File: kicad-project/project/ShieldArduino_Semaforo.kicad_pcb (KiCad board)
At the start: 4 copper layers, 68.6 x 53.3 mm, 108 parts, among them IC1 TLIN1039DDFRQ1, IC2 TPS563200DDCR, IC3 MCP4901T-E_MS, J2 Conn_01x18, K1 RELAY, P1 Power, P2 Analog, P3 Digital, P4 Digital, P5 CONN_01X01, P6 CONN_01X01, P7 CONN_01X01, P8 CONN_01X01, Q1 PMOS, Q2 NMOS, Q3 NMOS, Q4 NMOS, Q5 NMOS, U1 MCP2542FD-E/MF, U3 LM4040DBZ-2.0

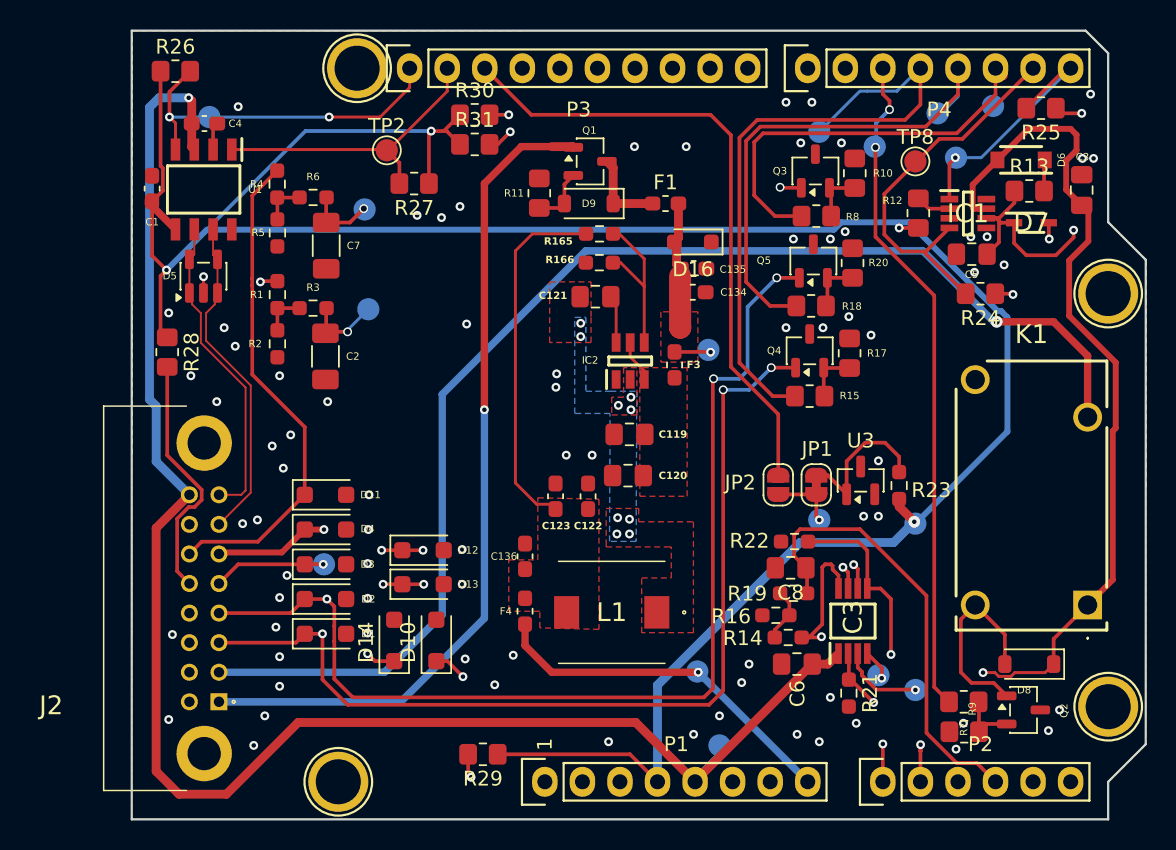
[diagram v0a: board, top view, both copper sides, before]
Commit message: kicad-pcb-silk_layer_cleanup
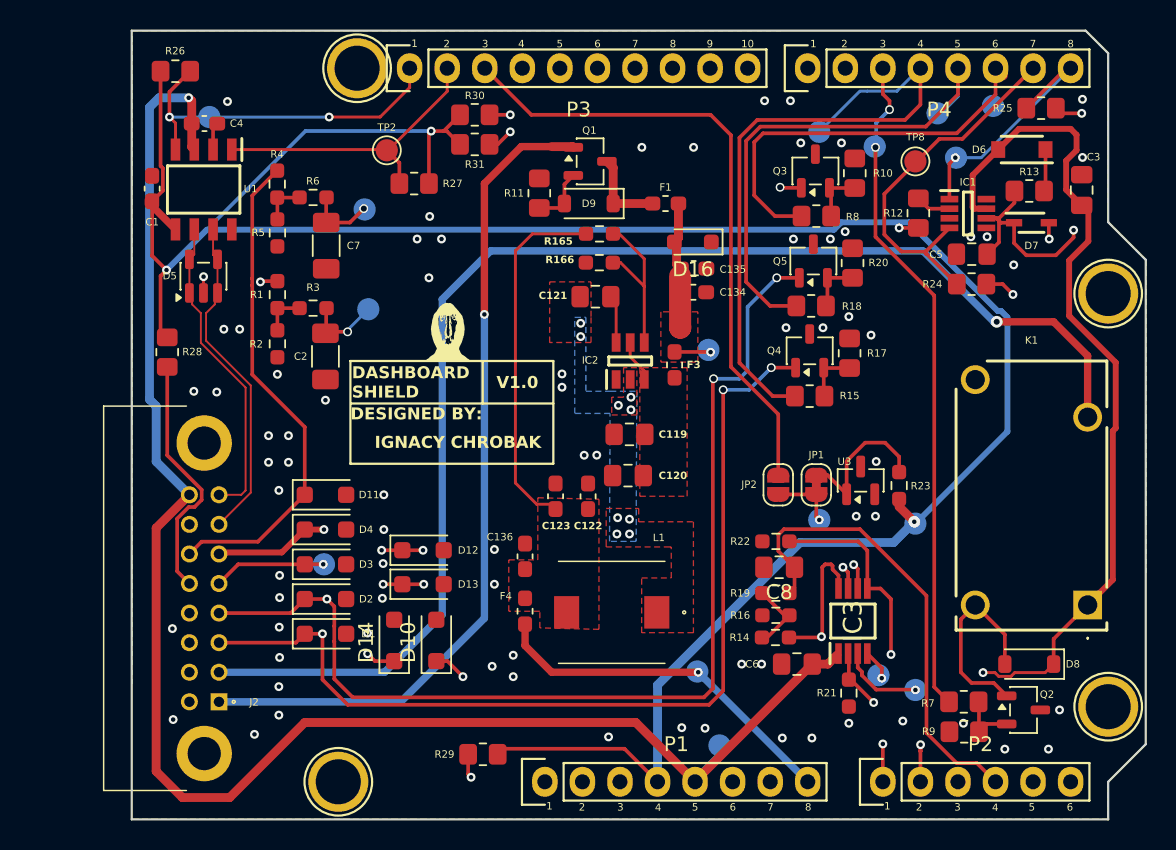
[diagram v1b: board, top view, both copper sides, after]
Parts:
- added G***: LOGO, Graphics:mandela, F.Cu at (132.4, 92.8)
- moved R22 1.26 mm to (154.6, 107.6)
- moved R19 1.20 mm to (154.6, 111.1)
- moved R24 0.88 mm to (167.8, 90.2)
- moved R14 0.86 mm to (154.5, 114.1)
- moved C8 0.78 mm to (154.8, 109.3)
- moved D6 0.70 mm to (171.2, 81.1)
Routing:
- net /relay_out: track 86.4 -> 90.1 mm
- net /STM_LDAC: track 70.8 -> 72.0 mm
- net /A3: track 30.6 -> 31.9 mm
- net Net-(R14-Pad2): track 3.68 -> 4.92 mm
- net +3.3V: track 249.6 -> 250.8 mm
- net /UART_RX: track 25.8 -> 25.0 mm
- net Net-(D6-K): track 2.12 -> 2.84 mm
- net GND: vias 79 -> 76
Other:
- board text added: "10"
- board text added: "2"
- board text added: "3"
- board text added: "4"
- board text added: "5"
- board text added: "6"
- board text added: "7"
- board text added: "8"
- board text added: "9"
- board text added: "DASHBOARD SHIELD"
- board text added: "DESIGNED BY:"
- board text added: "IGNACY CHROBAK"
- board text added: "V1.0"

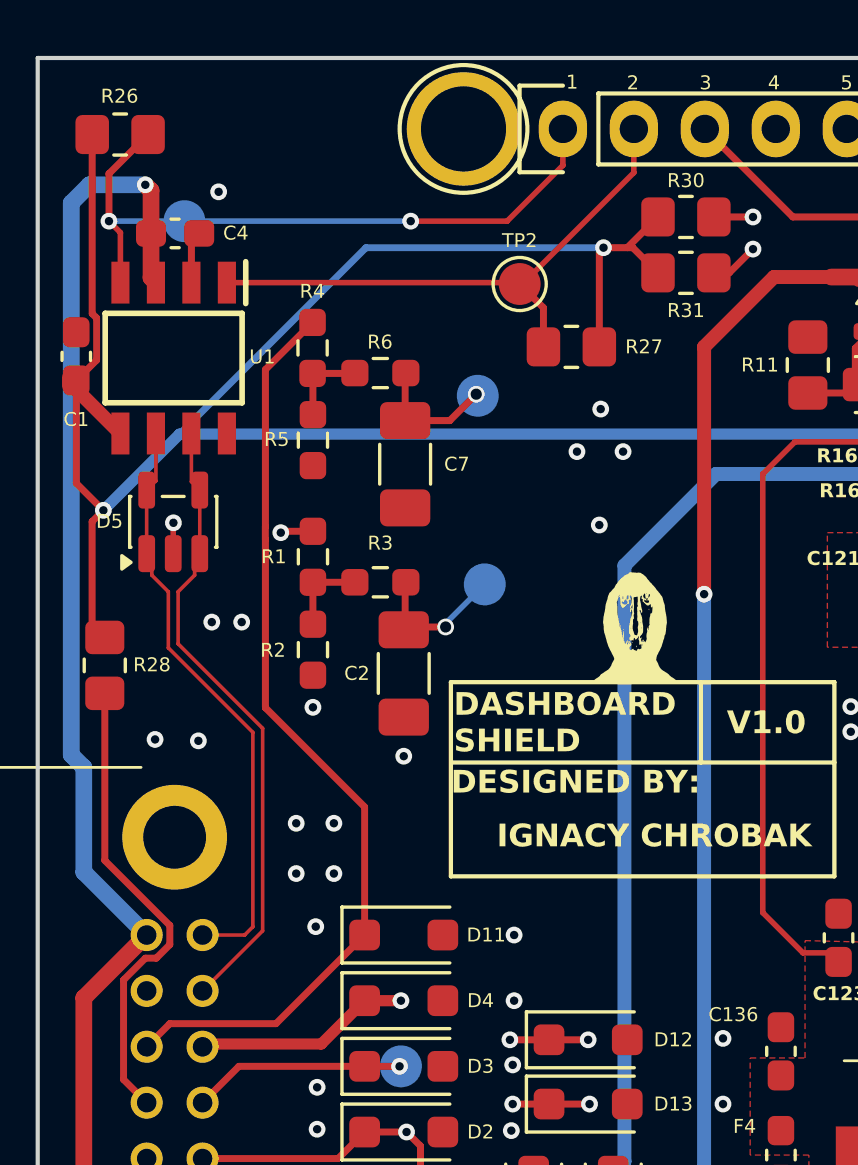
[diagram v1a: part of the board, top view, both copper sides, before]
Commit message: kicad-pcb-images
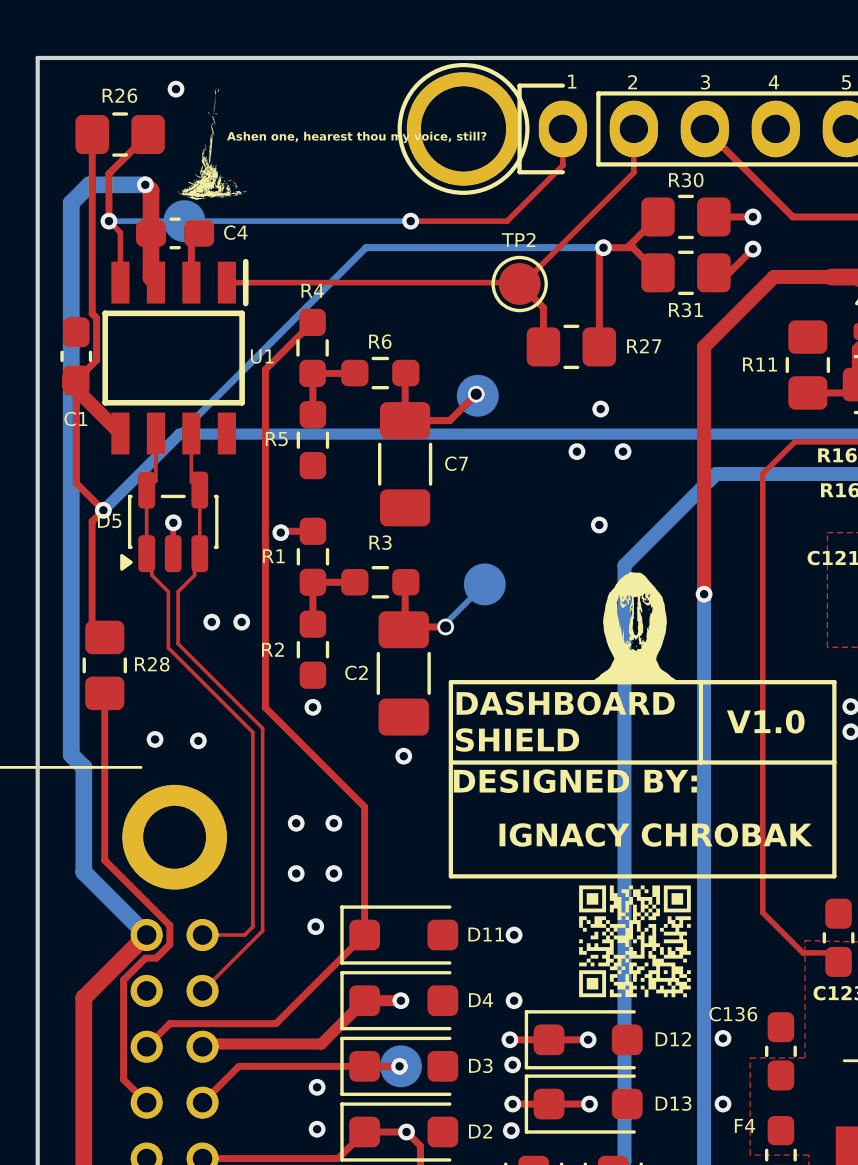
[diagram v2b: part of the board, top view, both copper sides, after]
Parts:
- added G***: LOGO, Graphics:bonfire, F.Cu at (117.2, 76.2)
- added G***: LOGO, Graphics:qr, F.Cu at (132.4, 104.6)
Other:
- board text added: "Ashen one, hearest thou my voice, still?"

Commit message: kicad-images
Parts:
- added G***: LOGO, Graphics:robot, F.Cu at (136.2, 104.4)
- moved G*** 4.90 mm to (137.3, 92.8)
- moved R6 0.24 mm to (123.0, 84.4)

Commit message: .
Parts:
- moved G*** 13.1 mm to (131.1, 116.5)

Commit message: kicad-pcb-relay_change
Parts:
- K1: footprint footprint:PR412V4501A -> footprint:RE034012
- moved K1 17.2 mm to (174.5, 94.7)
- moved R6 0.26 mm to (123.3, 84.4)
- moved C7 0.14 mm to (124.1, 87.7)
- moved R5 0.13 mm to (120.8, 86.8)
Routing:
- net /12V_in_protected: track 104.5 -> 127.8 mm
- net / relay_in: track 58.2 -> 64.1 mm, vias 1 -> 2
- net /relay_out: track 90.1 -> 85.1 mm
- net Net-(D8-A): track 13.7 -> 12.7 mm

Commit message: pcb-gerber-v1.0.0
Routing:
- net GND: vias 76 -> 81
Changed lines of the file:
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@@
 		(tags "D_SOD-123F")
 		(property "Reference" "D14"
-			(at -0.127 -1.905 90)
+			(at -2.7 0.05 180)
 			(layer "F.SilkS")
 			(effects
 				(font
-					(size 1 1)
-					(thickness 0.15)
+					(size 0.5 0.5)
+					(thickness 0.125)
 				)
 			)
@@
 		(tags "SOD-323")
 		(property "Reference" "D16"
-			(at 0 -1.85 180)
+			(at -0.05 1.35 180)
 			(layer "F.SilkS")
 			(effects
 				(font
-					(size 1 1)
-					(thickness 0.15)
+					(size 0.5 0.5)
+					(thickness 0.125)
 				)
 			)
@@
 		(tags "Integrated Circuit")
 		(property "Reference" "IC1"
-			(at 0 0 0)
+			(at 0.05 -2.225 0)
 			(layer "F.SilkS")
 			(effects
 				(font
-					(size 1.27 1.27)
-					(thickness 0.254)
+					(size 0.5 0.5)
+					(thickness 0.125)
 				)
 			)
@@
 		(tags "D_SOD-123F")
 		(property "Reference" "D10"
-			(at -0.127 -1.905 90)
+			(at -2.7 0 180)
 			(layer "F.SilkS")
 			(effects
 				(font
-					(size 1 1)
-					(thickness 0.15)
+					(size 0.5 0.5)
+					(thickness 0.125)
 				)
 			)
@@
 		(tags "Relay or Contactor")
 		(property "Reference" "K1"
-			(at -8.84 -3.78 90)
+			(at 2.55 -6.7 180)
 			(layer "F.SilkS")
 			(effects
 				(font
-					(size 1.27 1.27)
-					(thickness 0.254)
+					(size 0.5 0.5)
+					(thickness 0.125)
 				)
 			)
@@
 		(tags "capacitor handsolder")
 		(property "Reference" "C8"
-			(at 0 -1.68 0)
+			(at 2.3875 -0.05 0)
 			(layer "F.SilkS")
 			(effects
 				(font
-					(size 1 1)
-					(thickness 0.15)
+					(size 0.5 0.5)
+					(thickness 0.125)
 				)
 			)
@@
 		(tags "Integrated Circuit")
 		(property "Reference" "IC3"
-			(at 0 0 90)
+			(at -0.0125 2.225 180)
 			(layer "F.SilkS")
 			(effects
 				(font
-					(size 1.27 1.27)
-					(thickness 0.254)
+					(size 0.5 0.5)
+					(thickness 0.125)
 				)
 			)
@@
 			(layer "F.Fab")
 		)
-		(fp_text user "${REFERENCE}"
-			(at 0 0 90)
-			(layer "F.Fab")
-			(effects
-				(font
-					(size 1.27 1.27)
-					(thickness 0.254)
-				)
-			)
-		)
 		(pad "1" smd rect
 			(at -2.2 -0.975 180)
@@
 	)
 	(via
+		(at 162.498 84.365)
+		(size 0.6)
+		(drill 0.3)
+		(layers "F.Cu" "B.Cu")
+		(free yes)
+		(net 2)
+	)
+	(via
 		(at 170.648 88.865)
 		(size 0.6)
@@
 	)
 	(via
+		(at 167.998 115.365)
+		(size 0.6)
+		(drill 0.3)
+		(layers "F.Cu" "B.Cu")
+		(free yes)
+		(net 2)
+	)
+	(via
 		(at 159.998 105.865)
 		(size 0.6)
@@
 	)
 	(via
+		(at 163.498 114.865)
+		(size 0.6)
+		(drill 0.3)
+		(layers "F.Cu" "B.Cu")
+		(free yes)
+		(net 2)
+	)
+	(via
+		(at 173.998 80.865)
+		(size 0.6)
+		(drill 0.3)
+		(layers "F.Cu" "B.Cu")
+		(free yes)
+		(net 2)
+	)
+	(via
 		(at 159.098 109.315)
 		(size 0.6)
@@
 		(size 0.6)
 		(drill 0.3)
+		(layers "F.Cu" "B.Cu")
+		(free yes)
+		(net 2)
+	)
+	(via
+		(at 163.498 111.865)
+		(size 0.6)
+		(drill 0.3)
